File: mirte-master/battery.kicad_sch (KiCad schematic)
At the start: 2 parts, among them J17 PWR_IN

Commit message: mirte master parts jclpcb fixed
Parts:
- removed J17: PWR_IN, TerminalBlock_Phoenix:TerminalBlock_Phoenix_PT-1,5-2-5.0-H_1x02_P5.00mm_Horizontal, symbol Connector:Screw_Terminal_01x02
- added J23: sc, easyeda:CONN-TH_XY126V-5.0-2P, symbol Connector:Screw_Terminal_01x02
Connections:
- net +BATT: now also J23.2 (Pin_2)
- net -BATT: now also J23.1 (Pin_1)
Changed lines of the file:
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@@
-    )
-  )
-  (symbol (lib_id "Connector:Screw_Terminal_01x02") (at 54.61 78.74 0) (unit 1)
-    (in_bom yes) (on_board yes) (dnp no)
-    (property "Reference" "J17" (at 57.15 78.74 0)
-      (effects (font (size 1.27 1.27)) (justify left))
-    )
-    (property "Value" "PWR_IN" (at 57.15 81.28 0)
-      (effects (font (size 1.27 1.27)) (justify left))
-    )
-    (property "Footprint" "TerminalBlock_Phoenix:TerminalBlock_Phoenix_PT-1,5-2-5.0-H_1x02_P5.00mm_Horizontal" (at 54.61 78.74 0)
-      (effects (font (size 1.27 1.27)) hide)
-    )
-    (property "Datasheet" "~" (at 54.61 78.74 0)
-      (effects (font (size 1.27 1.27)) hide)
-    )
-    (property "LCSC" "C557646" (at 57.15 78.74 0)
-      (effects (font (size 1.27 1.27)) hide)
-    )
-    (pin "2")
-    (pin "1")
-    (instances
-      (project "mirte-master"
-        (path "/19794465-0368-488c-958e-83b02754ebd6/17ebe4c8-09bb-4699-976c-396d27e4a3f5/544a16a8-9ef3-43b3-aa0f-4bd972816cae/d3337f2d-26a9-4529-9bfc-380e6deefc08"
-          (reference "J17") (unit 1)
-        )
-        (path "/19794465-0368-488c-958e-83b02754ebd6/17ebe4c8-09bb-4699-976c-396d27e4a3f5/1289cdbf-c89c-46a5-93db-3249bdca7927"
-          (reference "J15") (unit 1)
-        )
-      )
     )
   )
@@
     )
   )
+  (symbol (lib_id "Connector:Screw_Terminal_01x02") (at 54.61 81.28 0) (mirror x) (unit 1)
+    (in_bom yes) (on_board yes) (dnp no)
+    (property "Reference" "J23" (at 57.15 81.28 0)
+      (effects (font (size 1.27 1.27)) (justify left))
+    )
+    (property "Value" "sc" (at 57.15 78.74 0)
+      (effects (font (size 1.27 1.27)) (justify left))
+    )
+    (property "Footprint" "easyeda:CONN-TH_XY126V-5.0-2P" (at 54.61 81.28 0)
+      (effects (font (size 1.27 1.27)) hide)
+    )
+    (property "Datasheet" "~" (at 54.61 81.28 0)
+      (effects (font (size 1.27 1.27)) hide)
+    )
+    (property "LCSC" "C557646" (at 54.61 81.28 0)
+      (effects (font (size 1.27 1.27)) hide)
+    )
+    (pin "2")
+    (pin "1")
+    (instances
+      (project "mirte-master"
+        (path "/19794465-0368-488c-958e-83b02754ebd6/17ebe4c8-09bb-4699-976c-396d27e4a3f5/cd5c3f96-e789-467d-9a0a-1e1e5a42c039"
+          (reference "J23") (unit 1)
+        )
+        (path "/19794465-0368-488c-958e-83b02754ebd6/17ebe4c8-09bb-4699-976c-396d27e4a3f5/1f6ba3bd-b93c-4e80-aba0-1409dab869f7"
+          (reference "J13") (unit 1)
+        )
+        (path "/19794465-0368-488c-958e-83b02754ebd6/17ebe4c8-09bb-4699-976c-396d27e4a3f5/1289cdbf-c89c-46a5-93db-3249bdca7927"
+          (reference "J18") (unit 1)
+        )
+      )
+    )
+  )
   (symbol (lib_id "Device:NetTie_2") (at 73.66 64.77 0) (mirror y) (unit 1)
-    (in_bom no) (on_board yes) (dnp no)
+    (in_bom no) (on_board no) (dnp no)
     (property "Reference" "NT1" (at 73.66 59.69 0)
       (effects (font (size 1.27 1.27)))

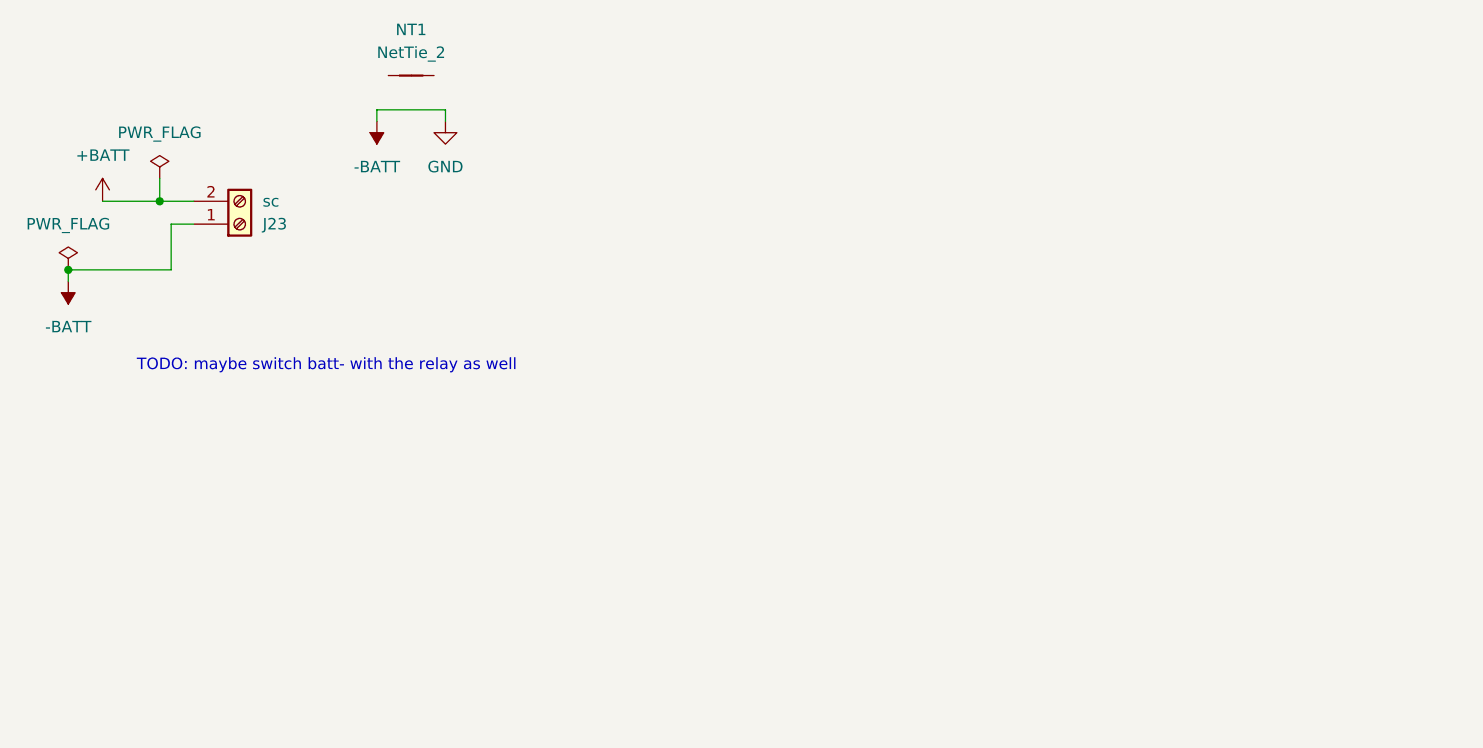
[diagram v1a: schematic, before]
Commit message: mirte-master schematic cleanup and readabilityimprovements
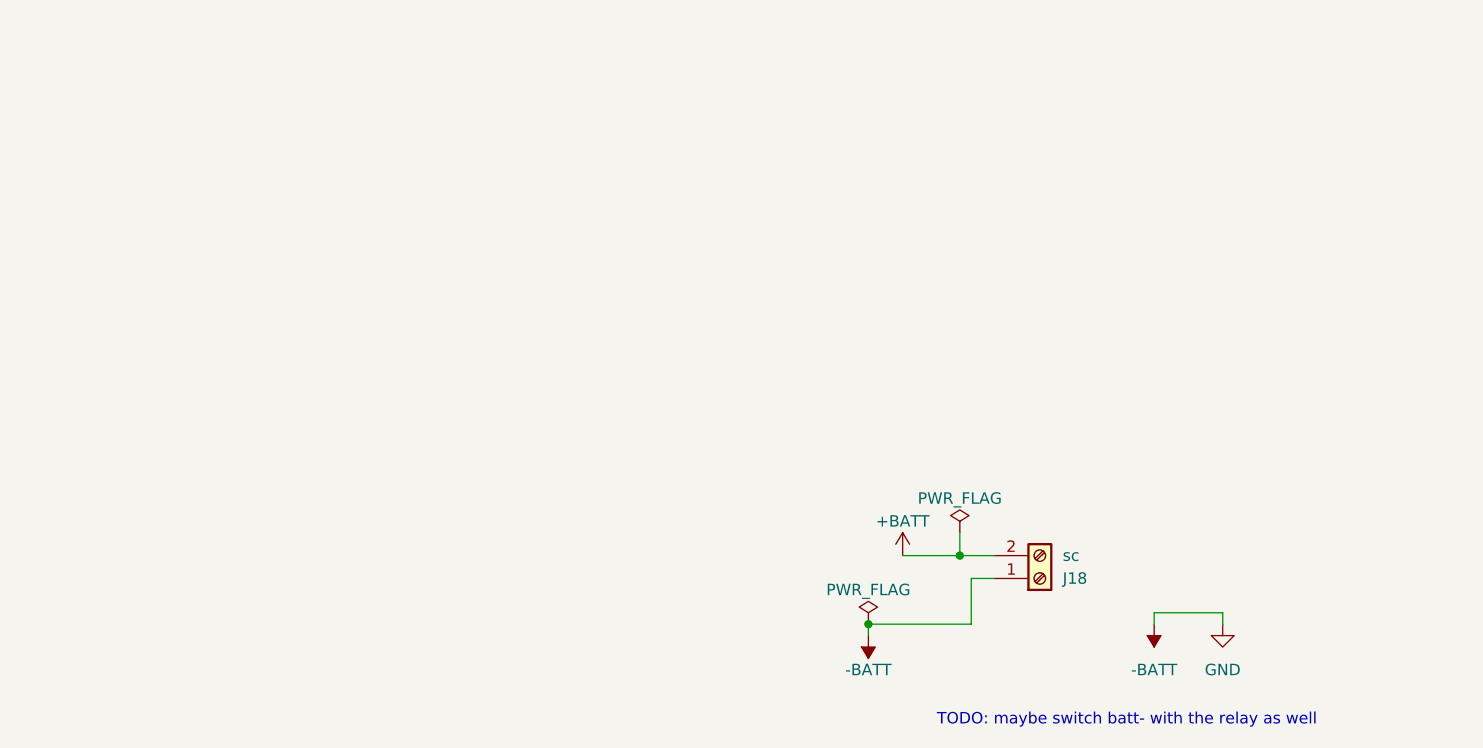
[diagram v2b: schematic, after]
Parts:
- removed NT1: NetTie_2, NetTie:NetTie-2_SMD_Pad0.5mm, symbol Device:NetTie_2
- renumbered J23 to J18
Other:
- title: (none) -> ${PROJECTNAME}
- moved on the sheet: J18
